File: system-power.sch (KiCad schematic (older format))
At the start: 36 parts, among them J1 Conn_01x02, J2 Conn_01x02, U1 MCP73831T-2ACI/OT, U2 BQ25504, U3 TPS63031

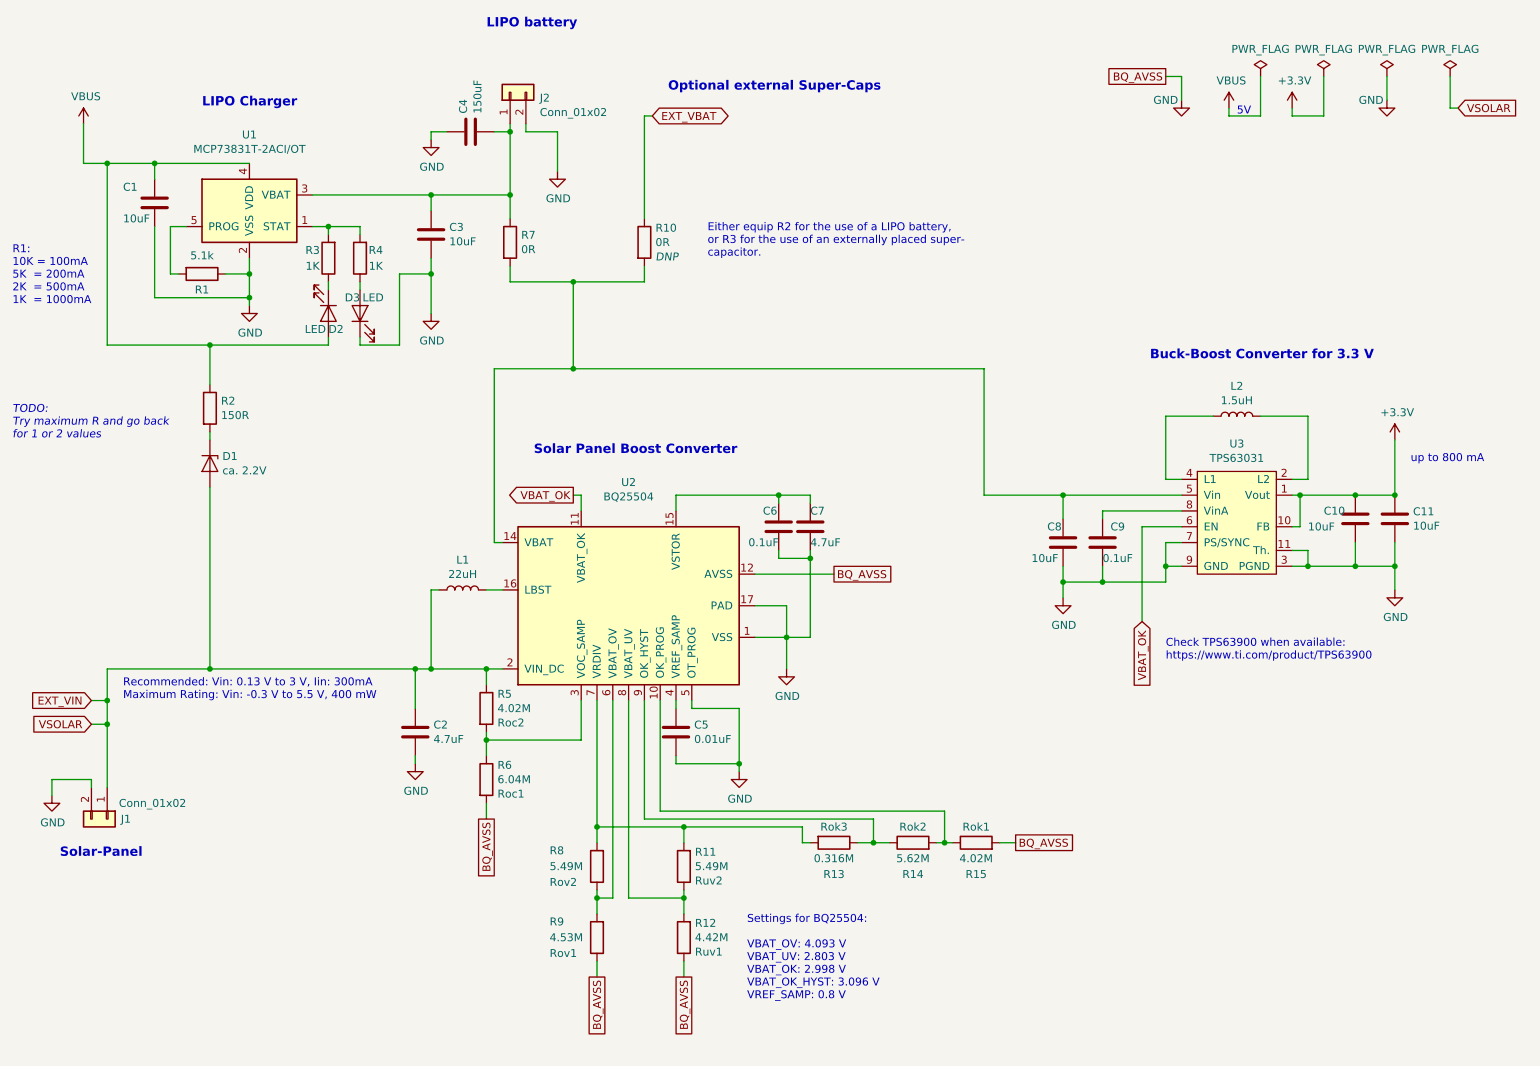
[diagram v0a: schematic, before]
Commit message: Changed notes on system power schematic
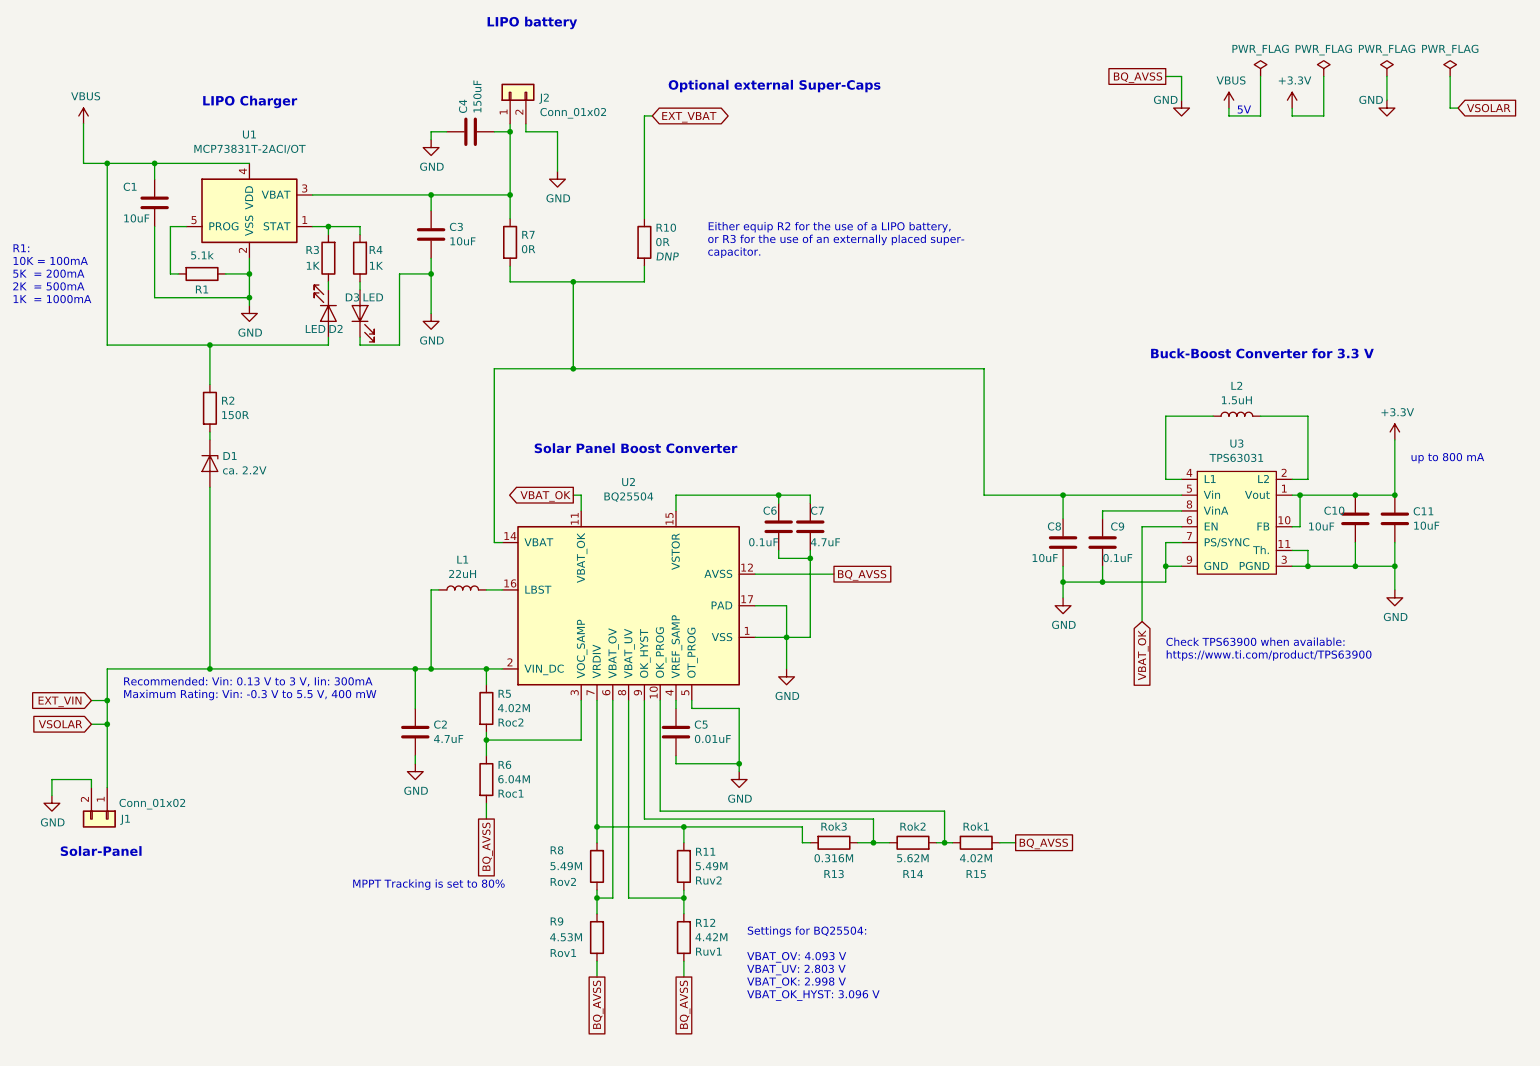
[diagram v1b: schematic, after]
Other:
- note added: "MPPT Tracking is set to 80%"
- note added: "Settings for BQ25504:\n\nVBAT_OV: 4.093 V\nVBAT_UV: 2.803 V\nVBAT_OK: 2.998 V\nVBAT_OK_HYST: 3.096 V"
- note removed: "Settings for BQ25504:\n\nVBAT_OV: 4.093 V\nVBAT_UV: 2.803 V\nVBAT_OK: 2.998 V\nVBAT_OK_HYST: 3.096 V\nVREF_SAMP: 0.8 V"
- note removed: "TODO:\nTry maximum R and go back\nfor 1 or 2 values"
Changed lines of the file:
@@
 $EndComp
 Text Notes 5600 6850 0    50   ~ 0
-Settings for BQ25504:\n\nVBAT_OV: 4.093 V\nVBAT_UV: 2.803 V\nVBAT_OK: 2.998 V\nVBAT_OK_HYST: 3.096 V\nVREF_SAMP: 0.8 V
+Settings for BQ25504:\n\nVBAT_OV: 4.093 V\nVBAT_UV: 2.803 V\nVBAT_OK: 2.998 V\nVBAT_OK_HYST: 3.096 V
 $Comp
 L power:PWR_FLAG #FLG02
@@
 	0    1    1    0
 $EndComp
-Text Notes 950  3300 0    50   Italic 0
-TODO:\nTry maximum R and go back\nfor 1 or 2 values
 Text GLabel 8100 4450 3    50   Input ~ 0
 VBAT_OK
@@
 Wire Wire Line
 	1550 4950 1550 5100
+Text Notes 3100 6150 0    50   ~ 0
+MPPT Tracking is set to 80%
 $EndSCHEMATC
